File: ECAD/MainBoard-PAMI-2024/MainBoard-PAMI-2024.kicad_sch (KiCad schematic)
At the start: 3 parts, among them U1 ESP32-S3-WROOM-1

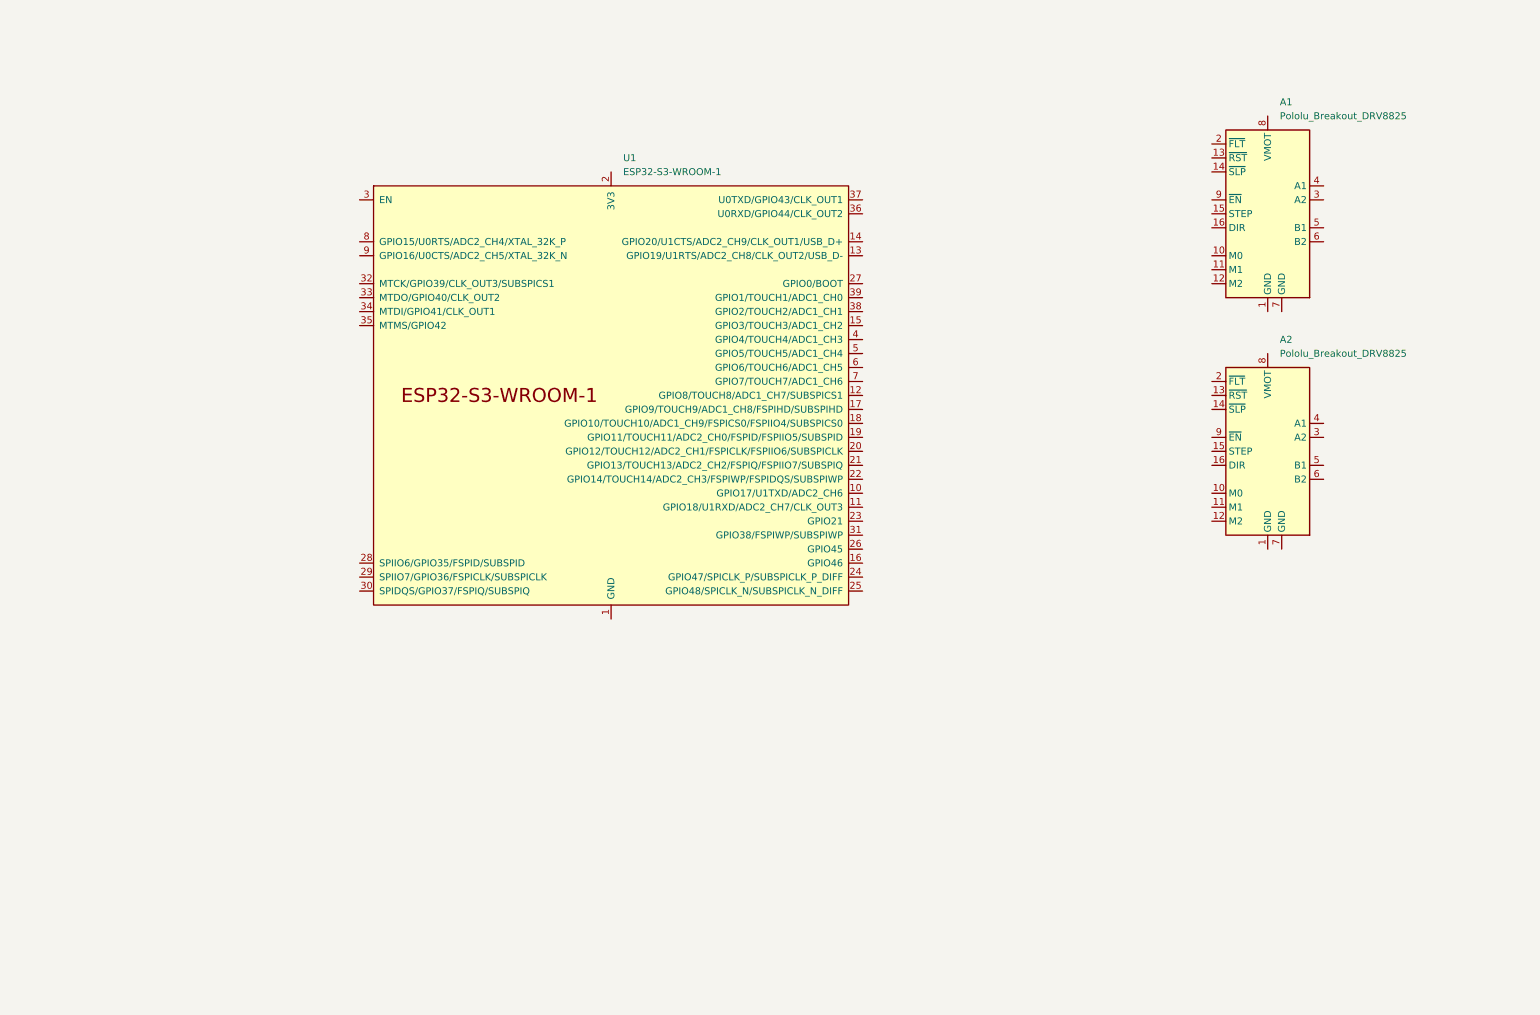
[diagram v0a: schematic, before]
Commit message: Modify Cut / Add components
Add :
- Connectors
- new Cut
- Regulator
- LEDs
- USB
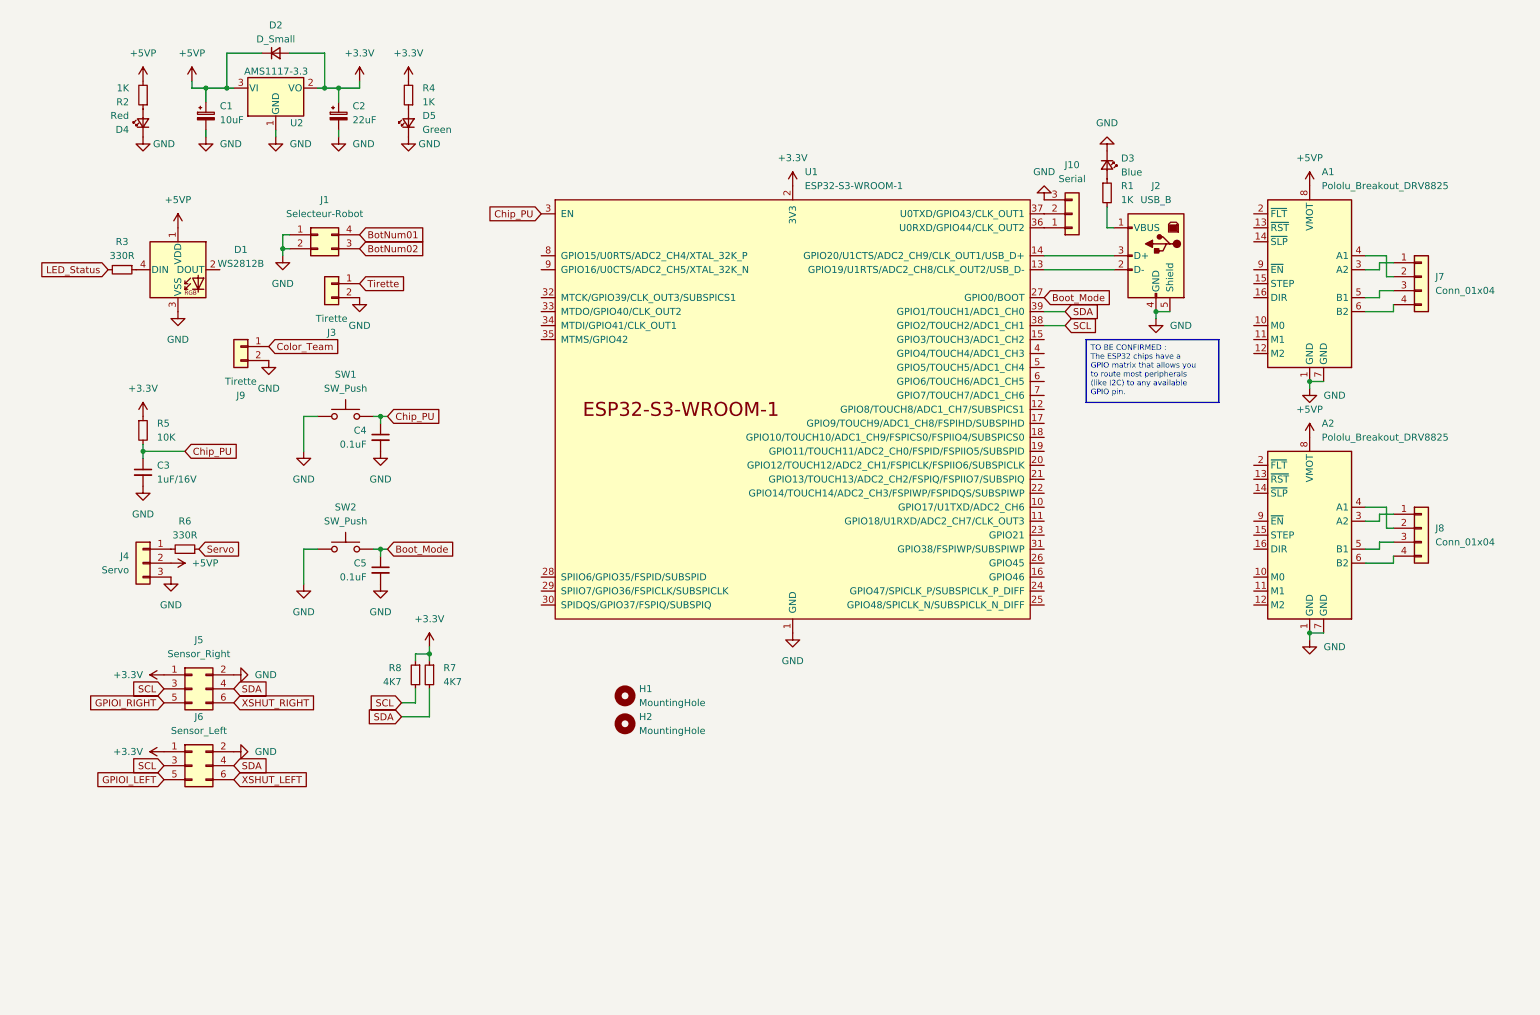
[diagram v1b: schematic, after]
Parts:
- added C1: 10uF, Capacitor_SMD:CP_Elec_5x5.4, symbol Device:C_Polarized_Small
- added C2: 22uF, Capacitor_Tantalum_SMD:CP_EIA-3528-12_Kemet-T_Pad1.50x2.35mm_HandSolder, symbol Device:C_Polarized_Small
- added C3: 1uF/16V, Capacitor_SMD:C_1206_3216Metric, symbol Device:C_Small
- added C4, C5: 0.1uF, Capacitor_SMD:C_1206_3216Metric, symbol Device:C_Small
- added D1: WS2812B, LED_SMD:LED_WS2812B_PLCC4_5.0x5.0mm_P3.2mm, symbol LED:WS2812B
- added D2: D_Small, Diode_SMD:D_SMA_Handsoldering, symbol Device:D_Small
- added D3: Blue, LED_SMD:LED_1206_3216Metric, symbol Device:LED_Small
- added D4: Red, LED_SMD:LED_1206_3216Metric, symbol Device:LED_Small
- added D5: Green, LED_SMD:LED_1206_3216Metric, symbol Device:LED_Small
- added H1, H2: MountingHole, MountingHole:MountingHole_3.2mm_M3, symbol Mechanical:MountingHole
- added J1: Selecteur-Robot, Connector_PinHeader_2.54mm:PinHeader_2x02_P2.54mm_Vertical, symbol Connector_Generic:Conn_02x02_Counter_Clockwise
- added J10: Serial, Connector_PinHeader_2.54mm:PinHeader_1x03_P2.54mm_Vertical, symbol Connector_Generic:Conn_01x03
- added J2: USB_B, Connector_USB:USB_B_Lumberg_2411_02_Horizontal, symbol Connector:USB_B
- added J3, J9: Tirette, Connector_PinHeader_2.54mm:PinHeader_1x02_P2.54mm_Vertical, symbol Connector_Generic:Conn_01x02
- added J4: Servo, Connector_PinHeader_2.54mm:PinHeader_1x03_P2.54mm_Vertical, symbol Connector_Generic:Conn_01x03
- added J5: Sensor_Right, Connector_IDC:IDC-Header_2x03_P2.54mm_Vertical, symbol Connector_Generic:Conn_02x03_Odd_Even
- added J6: Sensor_Left, Connector_IDC:IDC-Header_2x03_P2.54mm_Vertical, symbol Connector_Generic:Conn_02x03_Odd_Even
- added J7, J8: Conn_01x04, Connector_PinHeader_2.54mm:PinHeader_1x04_P2.54mm_Vertical, symbol Connector_Generic:Conn_01x04
- added R1, R2, R4: 1K, Resistor_SMD:R_1206_3216Metric_Pad1.30x1.75mm_HandSolder, symbol Device:R_Small
- added R3, R6: 330R, Resistor_SMD:R_1206_3216Metric_Pad1.30x1.75mm_HandSolder, symbol Device:R_Small
- added R5: 10K, Resistor_SMD:R_1206_3216Metric_Pad1.30x1.75mm_HandSolder, symbol Device:R_Small
- added R7, R8: 4K7, Resistor_SMD:R_1206_3216Metric_Pad1.30x1.75mm_HandSolder, symbol Device:R_Small
- added SW1, SW2: SW_Push, Button_Switch_SMD:SW_SPST_CK_RS282G05A3, symbol Switch:SW_Push
- added U2: AMS1117-3.3, Package_TO_SOT_SMD:SOT-223-3_TabPin2, symbol Regulator_Linear:AMS1117-3.3
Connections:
- net GND: now reaches A2.1 (GND)
- net GND: now also A1.1 (GND), A1.7 (GND), A2.7 (GND), U1.1 (GND), U1.40 (GND), U1.41 (GND), C1.2, C2.2, C3.2, C4.2, C5.2, D1.3 (VSS), D3.1 (K), D4.1 (K), D5.1 (K), J1.1 (Pin_1), J1.2 (Pin_2), J10.3 (Pin_3), J2.4 (GND), J2.5 (Shield), J3.2 (Pin_2), J4.3 (Pin_3), J5.2 (Pin_2), J6.2 (Pin_2), J9.2 (Pin_2), SW1.1, SW2.1, U2.1 (GND)
- net at A2.3 (A2): now also J8.1 (Pin_1)
- net at A2.4 (A1): now also J8.2 (Pin_2)
- net at A2.5 (B1): now also J8.3 (Pin_3)
- net at A2.6 (B2): now also J8.4 (Pin_4)
- net +5VP: now reaches A2.8 (VMOT)
- net +5VP: now also A1.8 (VMOT), C1.1, D1.1 (VDD), D2.1 (K), J4.2 (Pin_2), R2.2, U2.3 (VI)
- net at U1.13 (GPIO19/U1RTS/ADC2_CH8/CLK_OUT2/USB_D-): now also J2.2 (D-)
- net at U1.14 (GPIO20/U1CTS/ADC2_CH9/CLK_OUT1/USB_D+): now also J2.3 (D+)
- net +3.3V: now reaches U1.2 (3V3)
- net +3.3V: now also C2.1, D2.2 (A), J5.1 (Pin_1), J6.1 (Pin_1), R4.2, R5.1, R7.1, R8.1, U2.2 (VO)
- net Boot_Mode: now reaches U1.27 (GPIO0/BOOT)
- net Boot_Mode: now also C5.1, SW2.2
- net Chip_PU: now reaches U1.3 (EN)
- net Chip_PU: now also C3.1, C4.1, R5.2, SW1.2
- net at U1.36 (U0RXD/GPIO44/CLK_OUT2): now also J10.1 (Pin_1)
- net at U1.37 (U0TXD/GPIO43/CLK_OUT1): now also J10.2 (Pin_2)
- net SCL: now reaches U1.38 (GPIO2/TOUCH2/ADC1_CH1)
- net SCL: now also J5.3 (Pin_3), J6.3 (Pin_3), R8.2
- net SDA: now reaches U1.39 (GPIO1/TOUCH1/ADC1_CH0)
- net SDA: now also J5.4 (Pin_4), J6.4 (Pin_4), R7.2
- net at A1.3 (A2): now also J7.1 (Pin_1)
- net at A1.4 (A1): now also J7.2 (Pin_2)
- net at A1.5 (B1): now also J7.3 (Pin_3)
- net at A1.6 (B2): now also J7.4 (Pin_4)
- new net: J2.1 (VBUS), R1.2
- new net: D1.4 (DIN), R3.1
- new net: J4.1 (Pin_1), R6.2
- new net: D3.2 (A), R1.1
- new net: D4.2 (A), R2.1
- new net: D5.2 (A), R4.1
- new net BotNum01: J1.4 (Pin_4)
- new net BotNum02: J1.3 (Pin_3)
- new net Color_Team: J9.1 (Pin_1)
- new net GPIOI_LEFT: J6.5 (Pin_5)
- new net GPIOI_RIGHT: J5.5 (Pin_5)
- new net LED_Status: R3.2
- new net Servo: R6.1
- new net Tirette: J3.1 (Pin_1)
- new net XSHUT_LEFT: J6.6 (Pin_6)
- new net XSHUT_RIGHT: J5.6 (Pin_6)
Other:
- moved on the sheet: A1, A2, U1

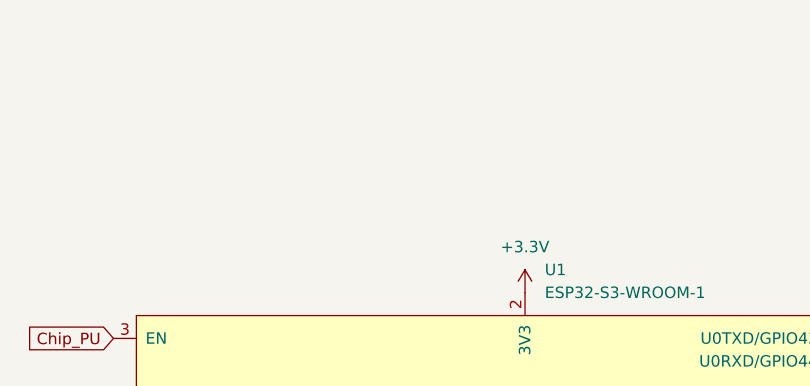
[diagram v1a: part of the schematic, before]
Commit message: add buzzer
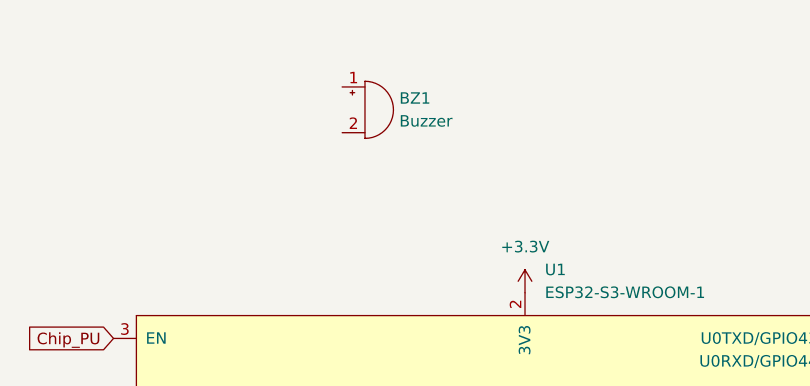
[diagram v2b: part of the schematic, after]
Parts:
- added BZ1: Buzzer, symbol Device:Buzzer
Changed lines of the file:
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@@
+    )
+  )
+  (symbol (lib_id "Device:Buzzer") (at 135.89 26.67 0) (unit 1)
+    (in_bom yes) (on_board yes) (dnp no) (fields_autoplaced)
+    (property "Reference" "BZ1" (at 139.7 25.4 0)
+      (effects (font (size 1.27 1.27)) (justify left))
+    )
+    (property "Value" "Buzzer" (at 139.7 27.94 0)
+      (effects (font (size 1.27 1.27)) (justify left))
+    )
+    (property "Footprint" "" (at 135.255 24.13 90)
+      (effects (font (size 1.27 1.27)) hide)
+    )
+    (property "Datasheet" "~" (at 135.255 24.13 90)
+      (effects (font (size 1.27 1.27)) hide)
+    )
+    (pin "1")
+    (pin "2")
+    (instances
+      (project "MainBoard-PAMI-2024"
+        (path "/d3e1aeb6-1412-4438-ac7d-372534bf2609"
+          (reference "BZ1") (unit 1)
+        )
+      )
     )
   )

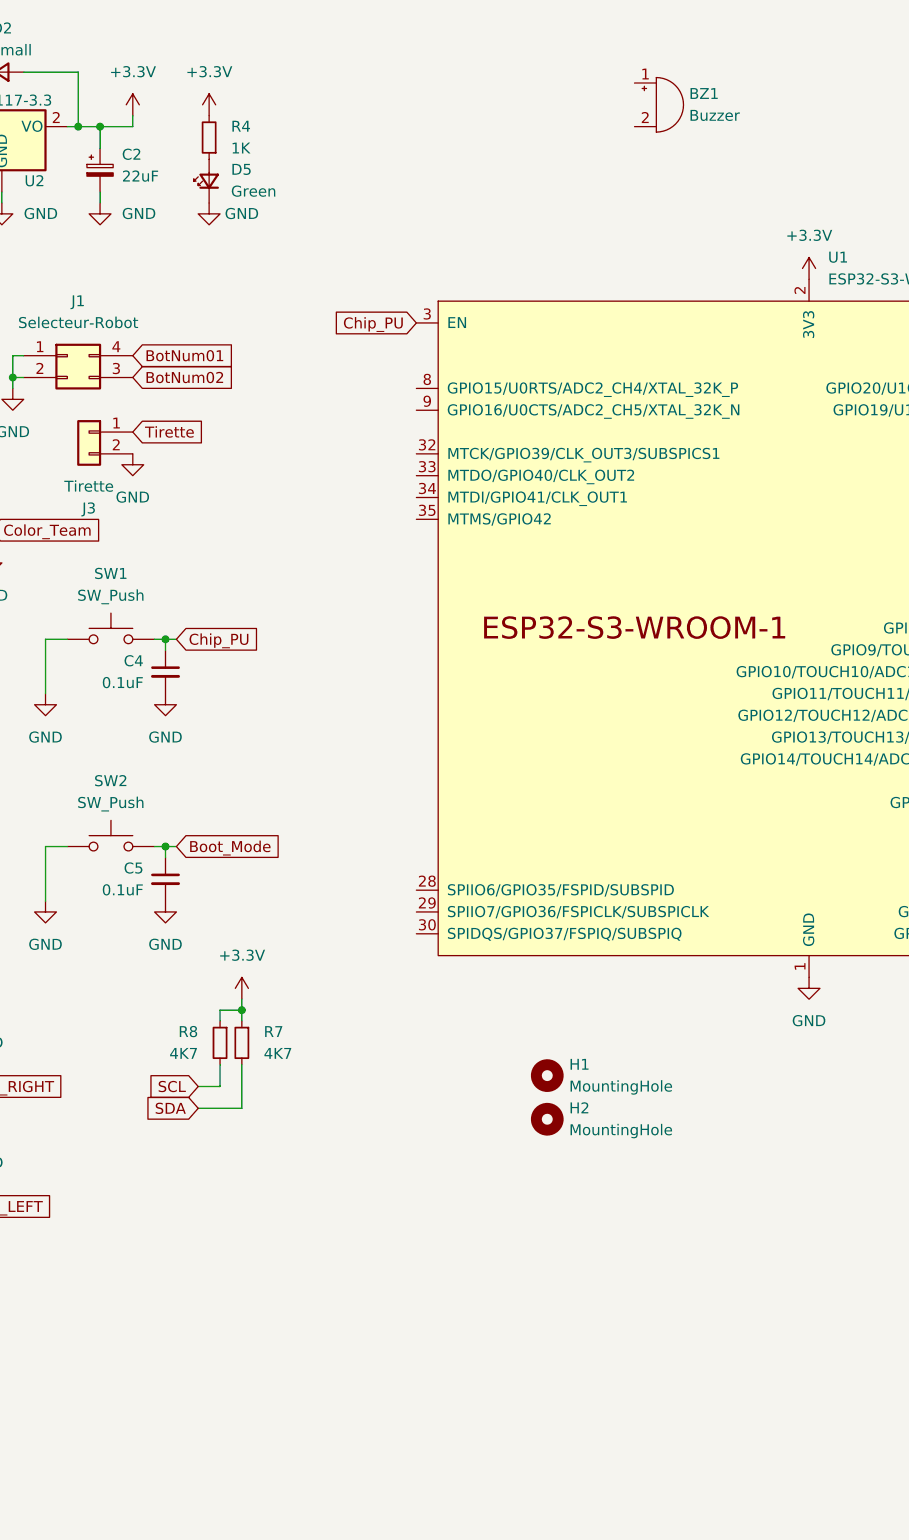
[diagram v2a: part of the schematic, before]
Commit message: add pen hole and opto sensor
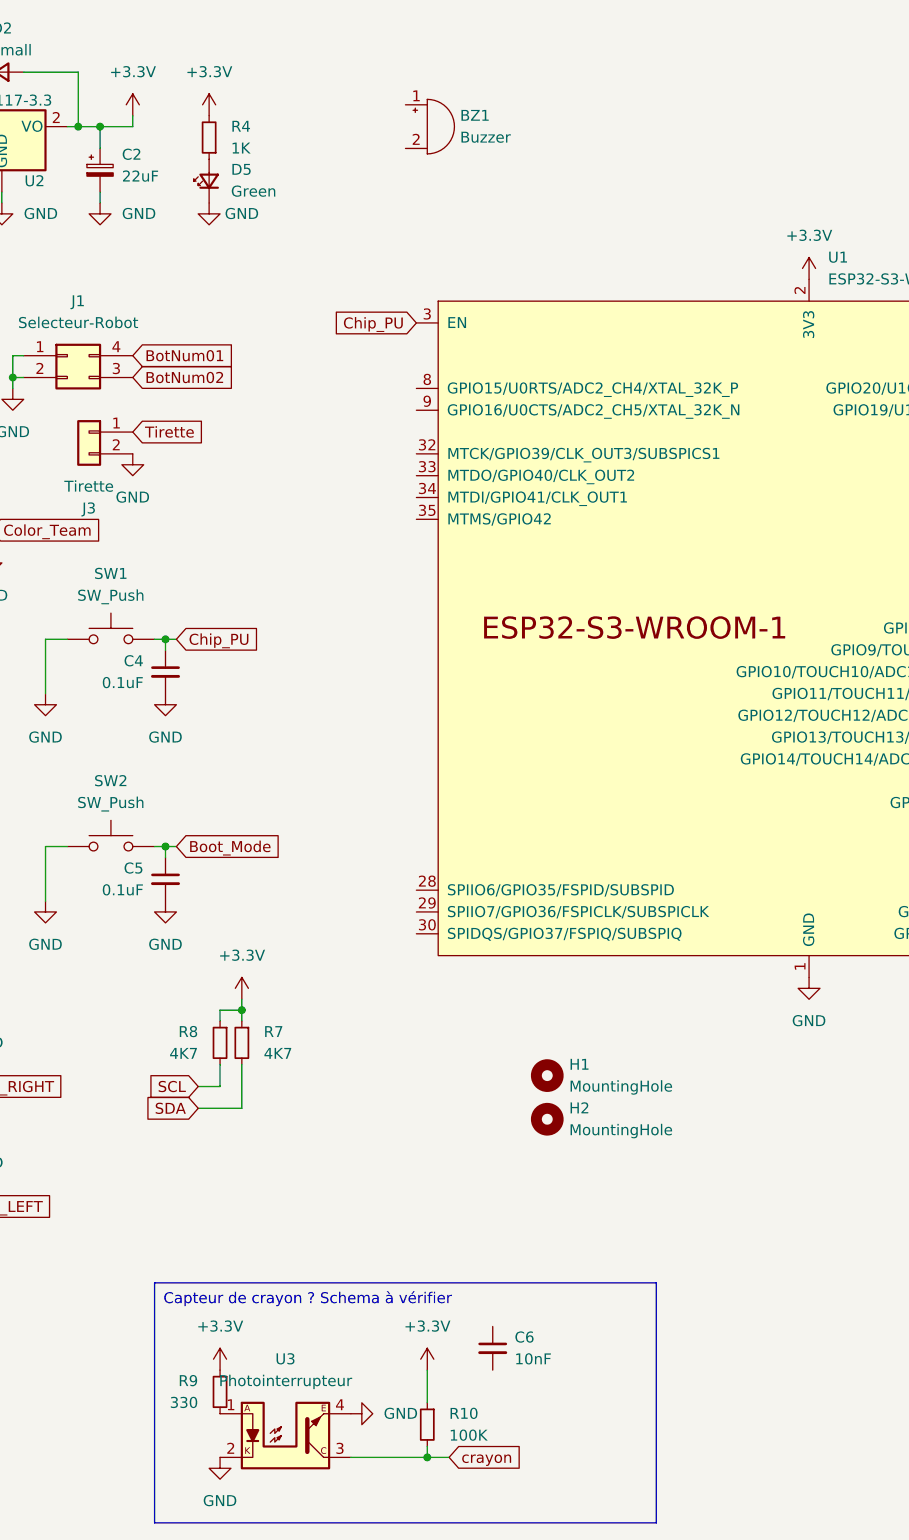
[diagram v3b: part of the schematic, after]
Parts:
- added C6: 10nF, symbol Device:C_Small
- added R10: 100K, Resistor_SMD:R_1206_3216Metric_Pad1.30x1.75mm_HandSolder, symbol Device:R_Small
- added R9: 330, Resistor_SMD:R_1206_3216Metric_Pad1.30x1.75mm_HandSolder, symbol Device:R_Small
- added U3: Photointerrupteur, symbol Sensor_Proximity:ITR9608-F
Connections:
- net +3.3V: now also R10.1, R9.1
- net GND: now also U3.2, U3.4
- new net: R9.2, U3.1
- new net crayon: R10.2, U3.3
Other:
- moved on the sheet: BZ1
